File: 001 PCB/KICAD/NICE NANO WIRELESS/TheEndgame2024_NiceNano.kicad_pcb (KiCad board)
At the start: 2 copper layers, 219 x 96.1 mm, 95 parts, among them J1 BATTERY_WIRES, SW10 SW_Push, SW11 SW_Push, SW12 SW_Push, SW13 SW_Push, SW14 SW_Push, SW15 SW_Push, SW16 SW_Push, SW17 SW_Push, SW18 SW_Push, SW19 SW_Push, SW2 SW_Push, SW20 SW_Push, SW21 SW_Push, SW22 SW_Push, SW23 SW_Push, SW24 SW_Push, SW25 SW_Push, SW26 SW_Push, SW27 SW_Push, SW28 SW_Push, SW29 SW_Push, SW3 SW_Push, SW30 SW_Push, SW31 SW_Push, SW32 SW_Push, SW33 SW_Push, SW34 SW_Push, SW35 SW_Push, SW36 SW_Push, SW37 SW_Push, SW38 PCM12SMTR, SW4 SW_Push, SW5 SW_Push, SW6 SW_Push, SW7 SW_Push, SW8 SW_Push, SW9 SW_Push, U2 nice!nano_v2

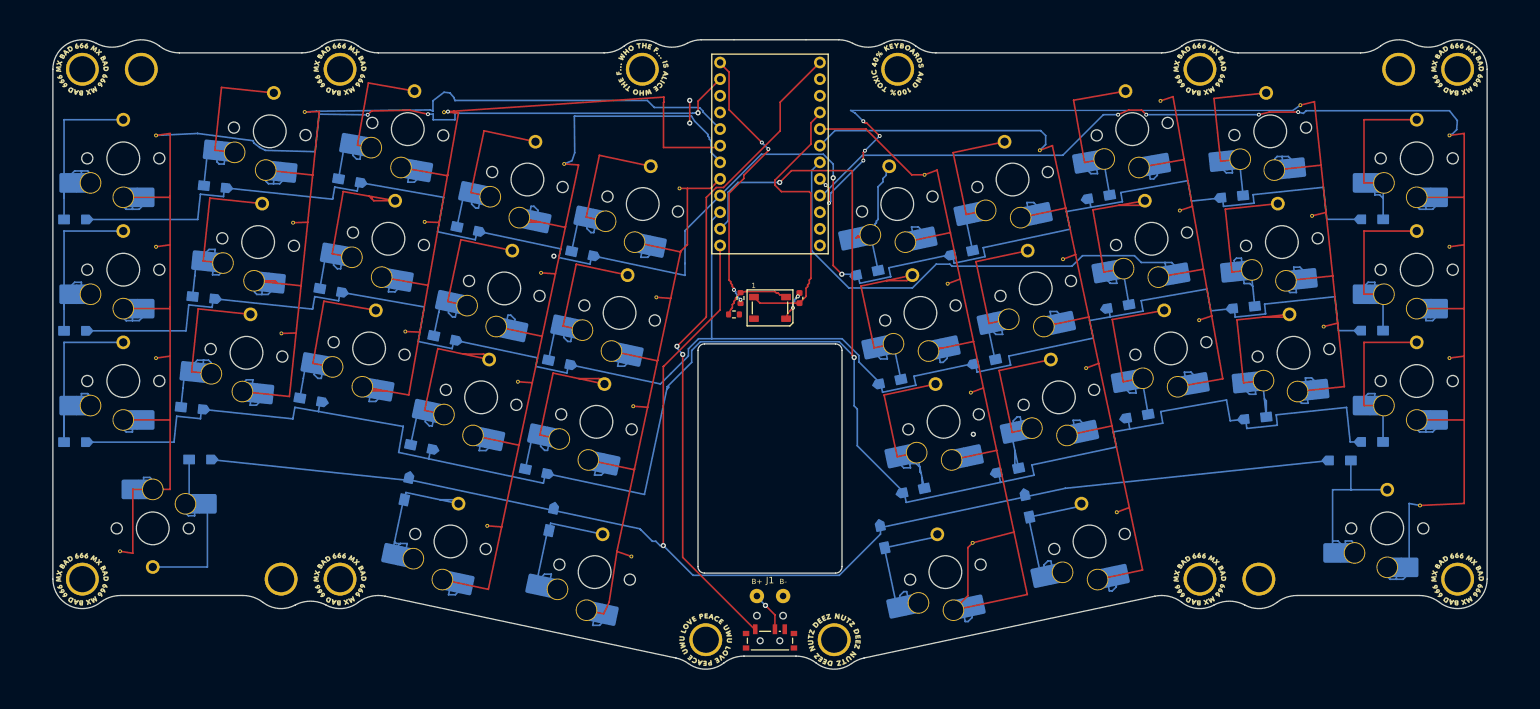
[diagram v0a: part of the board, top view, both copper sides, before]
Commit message: Widen key halves for controller clearance and add axial resistors
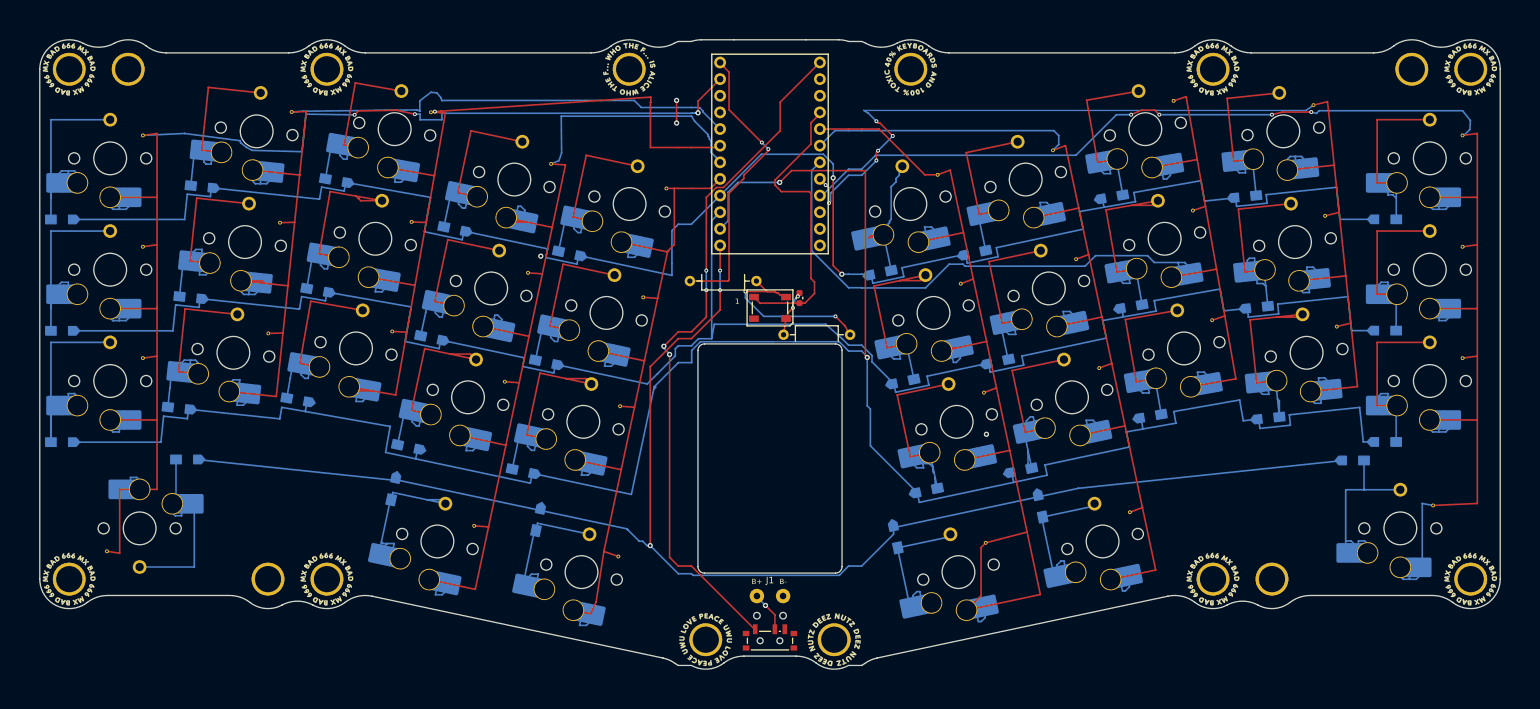
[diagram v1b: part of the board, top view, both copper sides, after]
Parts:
- R1, R2: footprint Resistor_SMD:R_0603_1608Metric -> NanoWireless:R_Axial_DIN0207_L6.3mm_D2.5mm_P10.16mm_Horizontal
- moved R2 18.0 mm to (162.2, 107.6), turned to 180 degrees
- moved R1 8.16 mm to (137.8, 99.4), turned to 0 degrees
- moved REF** 2.00 mm to (257.0, 144.9)
- moved D10 2.00 mm to (63.3, 85.0)
- moved D11 2.00 mm to (61.5, 101.9)
- moved D12 2.00 mm to (59.7, 118.8)
- moved D13 2.00 mm to (83.8, 84.1)
- moved D14 2.00 mm to (80.9, 100.8)
- moved D15 2.00 mm to (77.9, 117.6)
- moved D17 2.00 mm to (101.9, 91.5)
- moved D18 2.00 mm to (98.3, 108.1)
- moved D19 2.00 mm to (94.8, 124.8)
- moved D20 2.00 mm to (92.5, 131.1)
- moved D22 2.00 mm to (119.4, 95.2)
- moved D23 2.00 mm to (115.8, 111.8)
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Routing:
- net LED_DIN: track 11.3 -> 29.5 mm, vias 0 -> 2
- net row1: track 264.1 -> 270.8 mm
- net row3: track 229.1 -> 235.1 mm, vias 1 -> 3
- net row2: track 324.6 -> 330.6 mm
- net VBAT_SW: track 101.2 -> 105.2 mm, vias 2 -> 4
- net row0: track 265.1 -> 269.1 mm
- net gnd: track 8.11 -> 10.6 mm
- net col1: track 170.9 -> 172.9 mm
- net col0: track 227.9 -> 229.9 mm
- net col9: track 240.9 -> 242.9 mm
- net col8: track 192.9 -> 194.9 mm
- net col7: track 166.7 -> 168.7 mm
- net col6: track 171.5 -> 173.5 mm
- net col5: track 172.6 -> 174.6 mm
- net col3: track 169.7 -> 171.7 mm
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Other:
- board size 219 x 96.1 mm -> 223 x 96.1 mm
